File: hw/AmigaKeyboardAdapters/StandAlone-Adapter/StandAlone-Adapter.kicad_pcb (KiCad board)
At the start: 2 copper layers, 78.7 x 58.4 mm, 56 parts, among them J1 RJ10, J2 Conn_02x03_Odd_Even, P1 CONN_01X02, Q1 BSS138, Q2 BSS138, Q3 BSS138, U1 AZ1117-3.3, U3 STM32F401RCTx

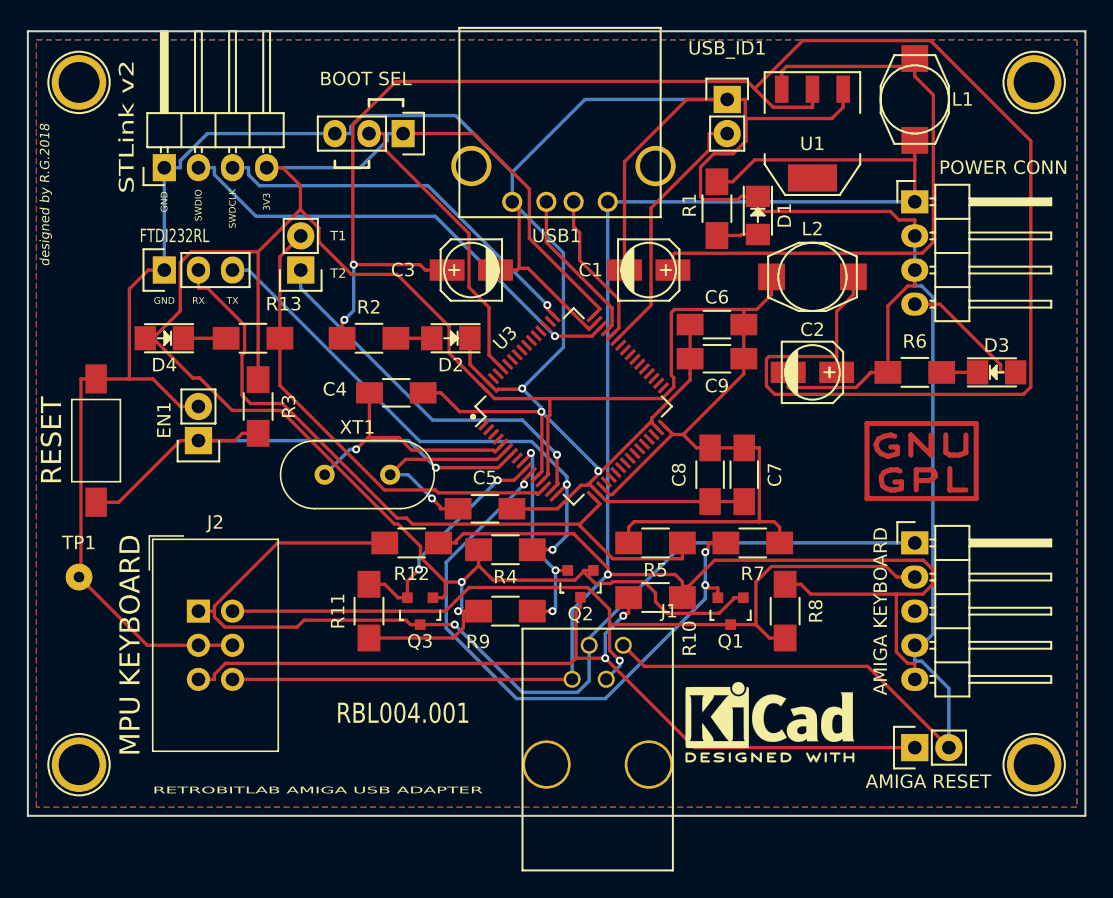
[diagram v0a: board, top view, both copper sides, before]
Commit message: Modified for Capacitors & Added some boot options
Replaced Electrolitic Capacitors with Tantalum ones. Added some
capacitor as in the evaluation board schematics. Added BOOT1 pin. Added
resistors for USB D+ D- lines. Increased the GND trace size to 0.35.
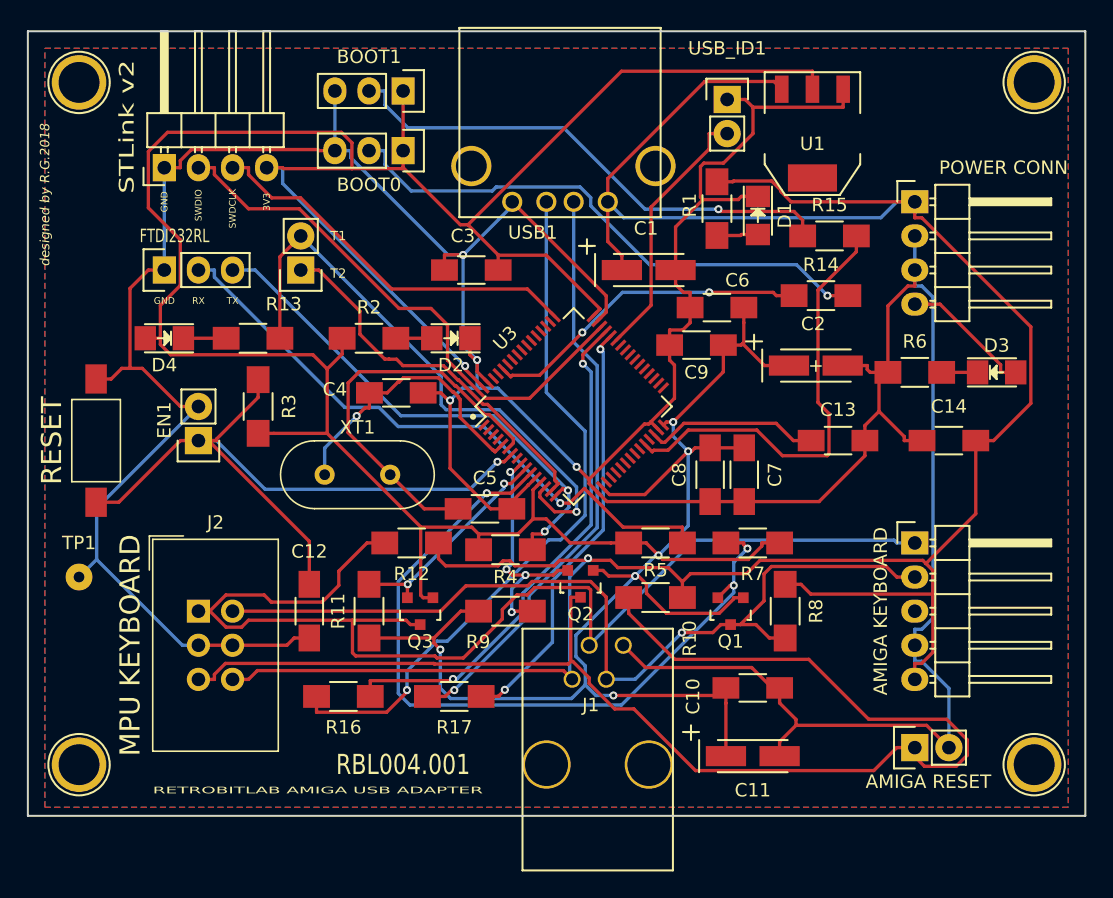
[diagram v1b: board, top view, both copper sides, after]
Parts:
- removed AMIGA: LOGO, RetroBitLab:amigaLogo_BW_31x12mm-SilkScreenBack
- removed GPL: Symbol_GNU-GPL_CopperTop_Small, Symbol:Symbol_GNU-GPL_CopperTop_Small
- removed L1, L2: 10uH, Inductors:SELF-WE-PD3S
- removed WB: LOGO, RetroBitLab:amigaWorkBench1-SIlkScreenBack
- removed kicad: KiCad-Logo2_5mm_SilkScreen, Symbol:KiCad-Logo2_5mm_SilkScreen
- added BOOT0: CONN_01X03, Pin_Headers:Pin_Header_Straight_1x03, F.Cu at (137.2, 74.9)
- added C10: 100n, Capacitors_SMD:C_1206_HandSoldering, F.Cu at (163.2, 114.9)
- added C11: 10u, Capacitors_Tantalum_SMD:TantalC_SizeA_EIA-3216_HandSoldering, F.Cu at (163.2, 120.0)
- added C12: 100n, Capacitors_SMD:C_1206_HandSoldering, F.Cu at (130.2, 109.2)
- added C13: 4.7u, Capacitors_SMD:C_1206_HandSoldering, F.Cu at (169.5, 96.5)
- added C14: 100n, Capacitors_SMD:C_1206_HandSoldering, F.Cu at (177.8, 96.5)
- added G***: LOGO, RetroBitLab:amigaWorkBench1-SIlkScreenBack, B.Cu at (138.4, 110.5)
- added G***: LOGO, RetroBitLab:amigaLogo_BW_31x12mm-SilkScreenBack, B.Cu at (151.1, 87.0)
- added R14: 10K, Resistors_SMD:R_1206_HandSoldering, F.Cu at (168.3, 85.7)
- added R15: 10K, Resistors_SMD:R_1206_HandSoldering, F.Cu at (168.9, 81.3)
- added R16: 12, Resistors_SMD:R_1206_HandSoldering, F.Cu at (132.7, 115.6)
- added R17: 12, Resistors_SMD:R_1206_HandSoldering, F.Cu at (141.0, 115.6)
- C1, C2: footprint Capacitors_SMD:c_elec_4x4.5 -> Capacitors_Tantalum_SMD:TantalC_SizeA_EIA-3216_HandSoldering
- C3: value 47u -> 100n; footprint Capacitors_SMD:c_elec_4x4.5 -> Capacitors_SMD:C_1206_HandSoldering
- R1, R13: value 330 -> 1.5K
- R10, R11, R12, R4, R5, R7, R8, R9: value 10k -> 10K
- R2: value 220 -> 1.5K
- R3: value 10K -> 22K
- R6: value 1K -> 1.5K
- moved BOOT1 3.17 mm to (137.2, 70.5)
- moved C9 1.83 mm to (159.0, 89.4)
- moved C6 1.27 mm to (160.5, 86.6)
- moved C2 0.57 mm to (167.9, 90.9)
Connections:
- AMIGA_KEYBOARD1 pad 5: VCC5V -> +5V
- BOOT1 pad 2: BOOT0 -> BOOT1
- C2 pad 1: Net-(C2-Pad1) -> VCC3V3
- C3 pad 1: Net-(C2-Pad1) -> VCC3V3
- EN1 pad 1: Net-(EN1-Pad1) -> NRST
- J1 pad 1: VCC5V -> +5V
- J2 pad 6: VCC5V -> +5V
- POWER1 pad 1: VCC5V -> +5V
- R1 pad 1: VCC5V -> +5V
- R10 pad 1: VCC5V -> +5V
- R12 pad 1: VCC5V -> +5V
- R2 pad 1: Net-(C2-Pad1) -> VCC3V3
- R3 pad 1: VCC3V3 -> NRST
- R3 pad 2: Net-(EN1-Pad1) -> VCC3V3
- R8 pad 1: VCC5V -> +5V
- RESET1 pad 1: Net-(EN1-Pad1) -> NRST
- U1 pad 2: Net-(C2-Pad1) -> VCC3V3
- U3 pad 28: (no net) -> Net-(R15-Pad2)
- U3 pad 30: (no net) -> Net-(C13-Pad1)
- U3 pad 60: BOOT0 -> Net-(R14-Pad1)
- U3 pad 7: Net-(EN1-Pad1) -> NRST
- USB1 pad 1: VCC5V -> +5V
- USB1 pad 2: USB_N -> Net-(R17-Pad2)
- USB1 pad 3: USB_P -> Net-(R16-Pad2)
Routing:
- net VCC5V: track 165.9 -> 0.00 mm, vias 1 -> 0
- net +5V: track 46.5 -> 195.0 mm, vias 0 -> 1
- net Net-(C2-Pad1): track 139.7 -> 0.00 mm, vias 2 -> 0
- net VCC3V3: track 241.5 -> 309.2 mm, vias 2 -> 7
- net NRST: track 0.00 -> 56.5 mm, vias 0 -> 1
- net Net-(R16-Pad2): track 0.00 -> 52.7 mm, vias 0 -> 1
- net Net-(R17-Pad2): track 0.00 -> 43.7 mm, vias 0 -> 1
- net Net-(EN1-Pad1): track 38.8 -> 0.00 mm, vias 1 -> 0
- net BOOT1: track 0.00 -> 38.1 mm, vias 0 -> 1
- net KBD_RESET: track 67.0 -> 100.9 mm, vias 2 -> 0
- net Net-(R15-Pad2): track 0.00 -> 33.3 mm
- net USB_P: track 11.8 -> 38.7 mm, vias 0 -> 2
- net Net-(R14-Pad1): track 0.00 -> 24.6 mm, vias 0 -> 2
- net USB_N: track 11.6 -> 31.8 mm, vias 0 -> 2
- net BOOT0: track 22.4 -> 41.3 mm, vias 0 -> 1
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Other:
- net class GND: trace_width 0.3 -> 0.35
- board text removed: "BOOT SEL"

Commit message: Modified some logo and silkscreen stuff
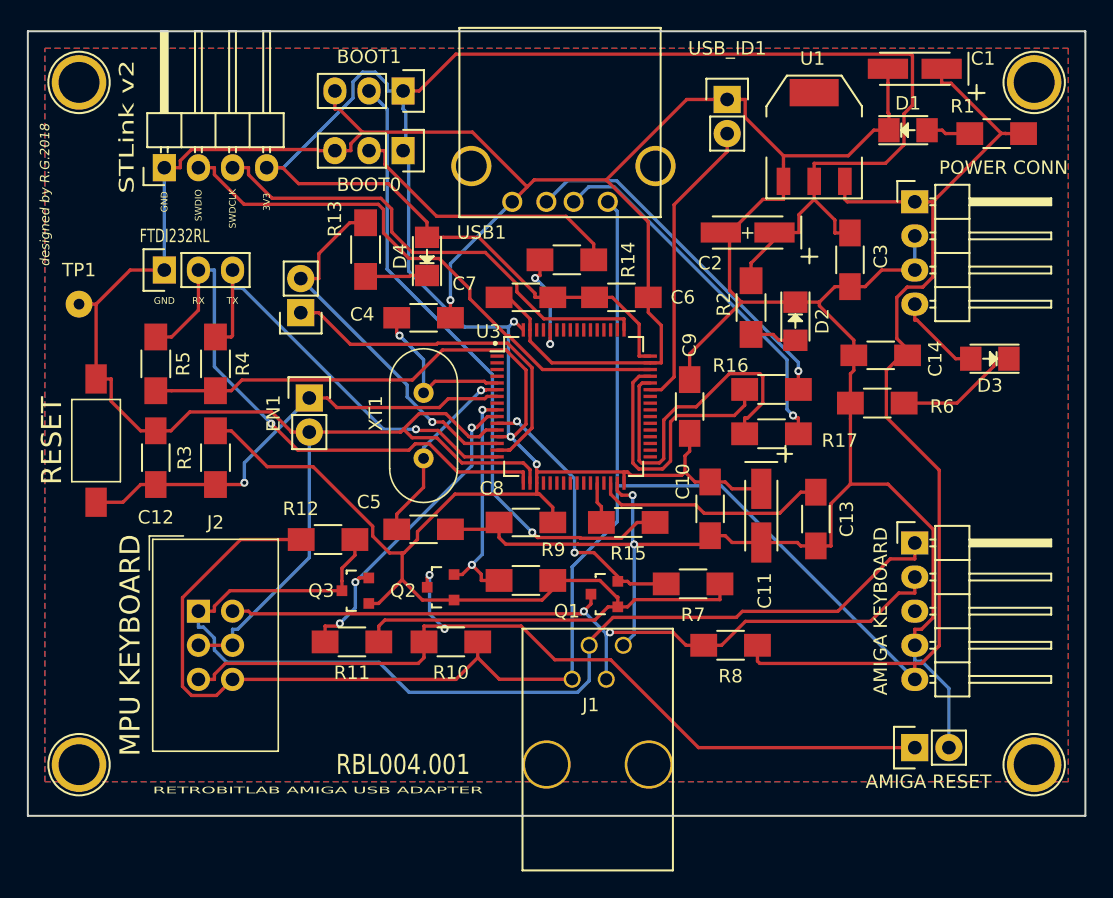
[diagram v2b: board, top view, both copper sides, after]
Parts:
- removed G***: LOGO, RetroBitLab:amigaWorkBench1-SIlkScreenBack
- removed G***: LOGO, RetroBitLab:amigaLogo_BW_31x12mm-SilkScreenBack
- added AMIGALOGO: LOGO, RetroBitLab:amigaLogo_BW_31x12mm, B.Cu at (152.4, 88.9)
- added WBLOGO: LOGO, RetroBitLab:amigaWorkBench1, B.Cu at (154.9, 104.1)
- moved R5 39.5 mm to (118.7, 90.8), turned to 90 degrees
- moved R16 39.2 mm to (164.6, 92.7), turned to 0 degrees
- moved R17 30.7 mm to (164.6, 96.0), turned to 0 degrees
- moved R2 28.5 mm to (163.1, 86.6), turned to 270 degrees
- moved C3 28.2 mm to (170.4, 83.1), turned to 270 degrees
- moved R15 26.1 mm to (153.9, 102.6), turned to 180 degrees
- moved D2 25.7 mm to (166.4, 87.6), turned to 270 degrees
- moved R4 25.6 mm to (123.2, 90.8), turned to 90 degrees
- moved C1 24.8 mm to (175.3, 68.8), turned to 180 degrees
- moved R1 21.6 mm to (181.4, 73.7), turned to 180 degrees
- moved C7 20.9 mm to (146.3, 85.9), turned to 0 degrees
- moved D4 20.5 mm to (138.9, 82.8), turned to 90 degrees
- moved TP1 20.3 mm to (113.0, 86.4)
- moved R14 19.1 mm to (149.4, 83.1)
- moved C11 17.9 mm to (163.8, 102.1), turned to 270 degrees
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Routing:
- net KBD_3v3_DATA: track 57.5 -> 21.2 mm, vias 3 -> 2
- net KBD_RESET: track 100.9 -> 66.0 mm, vias 0 -> 2
- net Net-(R15-Pad2): track 33.3 -> 3.07 mm
- net Net-(R16-Pad2): track 52.7 -> 27.0 mm
- net NRST: track 56.5 -> 34.6 mm
- net BOOT0: track 41.3 -> 21.4 mm, vias 1 -> 0
- net USB_P: track 38.7 -> 20.8 mm, vias 2 -> 0
- net Net-(R14-Pad1): track 24.6 -> 8.04 mm
- net Net-(R17-Pad2): track 43.7 -> 27.7 mm
- net TP1: track 43.8 -> 27.9 mm
- net Net-(C5-Pad1): track 29.9 -> 14.2 mm, vias 0 -> 1
- net BOOT1: track 38.1 -> 47.7 mm
- net Net-(C4-Pad1): track 21.4 -> 12.3 mm
- net KBD_CLOCK: track 88.3 -> 79.8 mm
- net KBD_3v3_CLOCK: track 16.5 -> 24.4 mm, vias 2 -> 3
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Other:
- net class +5V: trace_width 0.3 -> 0.35
- net class Default: trace_width 0.25 -> 0.3
- net class GND: trace_width 0.35 -> 0.4
- net class VCC3V3: trace_width 0.3 -> 0.35
- net class VCC5V: trace_width 0.3 -> 0.35
- board text removed: "T1"
- board text removed: "T2"

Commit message: Added GNU GPL LOGO on silkscreen top
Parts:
- added REF**: Symbol_GNU-GPL_CopperTop_Small, RetroBitLab:Symbol_GNU-GPL_SilkScreen_Small, F.Cu at (177.8, 99.1)
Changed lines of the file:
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@@
     (tracks 646)
     (zones 0)
-    (modules 62)
+    (modules 63)
     (nets 34)
   )
@@
       (xy 1.307739 4.732367)) (layer B.SilkS) (width 0.01))
   )
+  (module RetroBitLab:Symbol_GNU-GPL_SilkScreen_Small (layer F.Cu)
+    (at 177.8 99.06)
+    (descr "Symbol, GNU-GPL, Copper Top, Small,")
+    (tags "Symbol, GNU-GPL, Copper Top, Small,")
+    (fp_text reference REF** (at 0.50038 -6.79958) (layer F.SilkS)
+      (effects (font (size 1 1) (thickness 0.15)))
+    )
+    (fp_text value Symbol_GNU-GPL_CopperTop_Small (at -0.09906 6.10108) (layer F.Fab)
+      (effects (font (size 1 1) (thickness 0.15)))
+    )
+    (fp_line (start 2.10058 0.29972) (end 2.10058 1.89992) (layer F.SilkS) (width 0.381))
+    (fp_line (start 2.10058 1.89992) (end 3.29946 1.89992) (layer F.SilkS) (width 0.381))
+    (fp_line (start -0.39878 1.89992) (end -0.39878 0.39878) (layer F.SilkS) (width 0.381))
+    (fp_line (start -0.39878 0.39878) (end 0.50038 0.39878) (layer F.SilkS) (width 0.381))
+    (fp_line (start 0.50038 0.39878) (end 0.70104 0.39878) (layer F.SilkS) (width 0.381))
+    (fp_line (start 0.70104 0.39878) (end 0.89916 0.50038) (layer F.SilkS) (width 0.381))
+    (fp_line (start 0.89916 0.50038) (end 1.00076 0.70104) (layer F.SilkS) (width 0.381))
+    (fp_line (start 1.00076 0.70104) (end 1.00076 0.89916) (layer F.SilkS) (width 0.381))
+    (fp_line (start 1.00076 0.89916) (end 0.8001 1.09982) (layer F.SilkS) (width 0.381))
+    (fp_line (start 0.8001 1.09982) (end 0.50038 1.19888) (layer F.SilkS) (width 0.381))
+    (fp_line (start 0.50038 1.19888) (end -0.39878 1.19888) (layer F.SilkS) (width 0.381))
+    (fp_line (start -1.6002 0.50038) (end -1.80086 0.39878) (layer F.SilkS) (width 0.381))
+    (fp_line (start -1.80086 0.39878) (end -2.30124 0.39878) (layer F.SilkS) (width 0.381))
+    (fp_line (start -2.30124 0.39878) (end -2.60096 0.50038) (layer F.SilkS) (width 0.381))
+    (fp_line (start -2.60096 0.50038) (end -2.79908 0.59944) (layer F.SilkS) (width 0.381))
+    (fp_line (start -2.79908 0.59944) (end -2.99974 0.89916) (layer F.SilkS) (width 0.381))
+    (fp_line (start -2.99974 0.89916) (end -2.99974 1.19888) (layer F.SilkS) (width 0.381))
+    (fp_line (start -2.99974 1.19888) (end -2.90068 1.6002) (layer F.SilkS) (width 0.381))
+    (fp_line (start -2.90068 1.6002) (end -2.60096 1.80086) (layer F.SilkS) (width 0.381))
+    (fp_line (start -2.60096 1.80086) (end -2.30124 1.89992) (layer F.SilkS) (width 0.381))
+    (fp_line (start -2.30124 1.89992) (end -1.99898 1.89992) (layer F.SilkS) (width 0.381))
+    (fp_line (start -1.99898 1.89992) (end -1.50114 1.80086) (layer F.SilkS) (width 0.381))
+    (fp_line (start -1.50114 1.80086) (end -1.50114 1.30048) (layer F.SilkS) (width 0.381))
+    (fp_line (start -1.50114 1.30048) (end -1.99898 1.30048) (layer F.SilkS) (width 0.381))
+    (fp_line (start 1.80086 -2.19964) (end 1.80086 -0.89916) (layer F.SilkS) (width 0.381))
+    (fp_line (start 1.80086 -0.89916) (end 2.10058 -0.70104) (layer F.SilkS) (width 0.381))
+    (fp_line (start 2.10058 -0.70104) (end 2.4003 -0.70104) (layer F.SilkS) (width 0.381))
+    (fp_line (start 2.4003 -0.70104) (end 2.79908 -0.70104) (layer F.SilkS) (width 0.381))
+    (fp_line (start 2.79908 -0.70104) (end 3.0988 -0.8001) (layer F.SilkS) (width 0.381))
+    (fp_line (start 3.0988 -0.8001) (end 3.29946 -0.89916) (layer F.SilkS) (width 0.381))
+    (fp_line (start 3.29946 -0.89916) (end 3.29946 -2.19964) (layer F.SilkS) (width 0.381))
+    (fp_line (start -0.8001 -0.70104) (end -0.8001 -2.19964) (layer F.SilkS) (width 0.381))
+    (fp_line (start -0.8001 -2.19964) (end 0.70104 -0.70104) (layer F.SilkS) (width 0.381))
+    (fp_line (start 0.70104 -0.70104) (end 0.70104 -2.19964) (layer F.SilkS) (width 0.381))
+    (fp_line (start -1.99898 -2.10058) (end -2.30124 -2.19964) (layer F.SilkS) (width 0.381))
+    (fp_line (start -2.30124 -2.19964) (end -2.79908 -2.10058) (layer F.SilkS) (width 0.381))
+    (fp_line (start -2.79908 -2.10058) (end -3.2004 -1.89992) (layer F.SilkS) (width 0.381))
+    (fp_line (start -3.2004 -1.89992) (end -3.40106 -1.50114) (layer F.SilkS) (width 0.381))
+    (fp_line (start -3.40106 -1.50114) (end -3.29946 -1.09982) (layer F.SilkS) (width 0.381))
+    (fp_line (start -3.29946 -1.09982) (end -2.99974 -0.8001) (layer F.SilkS) (width 0.381))
+    (fp_line (start -2.99974 -0.8001) (end -2.49936 -0.59944) (layer F.SilkS) (width 0.381))
+    (fp_line (start -2.49936 -0.59944) (end -1.80086 -0.8001) (layer F.SilkS) (width 0.381))
+    (fp_line (start -1.80086 -0.8001) (end -1.80086 -1.30048) (layer F.SilkS) (width 0.381))
+    (fp_line (start -1.80086 -1.30048) (end -2.30124 -1.30048) (layer F.SilkS) (width 0.381))
+    (fp_line (start -4.064 -3.048) (end 4.064 -3.048) (layer F.SilkS) (width 0.381))
+    (fp_line (start 4.064 -3.048) (end 4.064 2.54) (layer F.SilkS) (width 0.381))
+    (fp_line (start 4.064 2.54) (end -4.064 2.54) (layer F.SilkS) (width 0.381))
+    (fp_line (start -4.064 2.54) (end -4.064 -3.048) (layer F.SilkS) (width 0.381))
+  )
   (gr_circle (center 144.018 89.281) (end 143.9545 89.2175) (layer F.SilkS) (width 0.2))

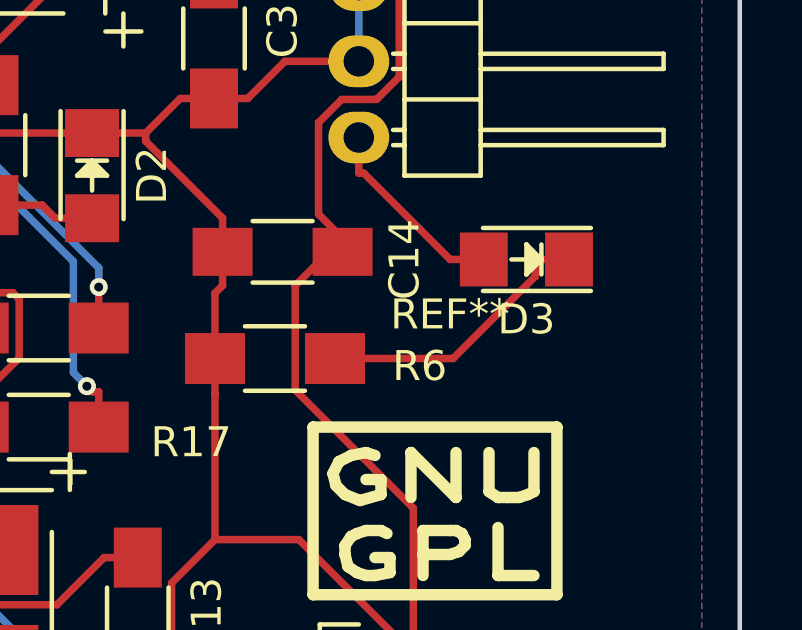
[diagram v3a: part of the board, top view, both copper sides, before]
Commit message: Changed the capacitors for Crystal Oscillator. From 22pf to 20pf for 8Mhz
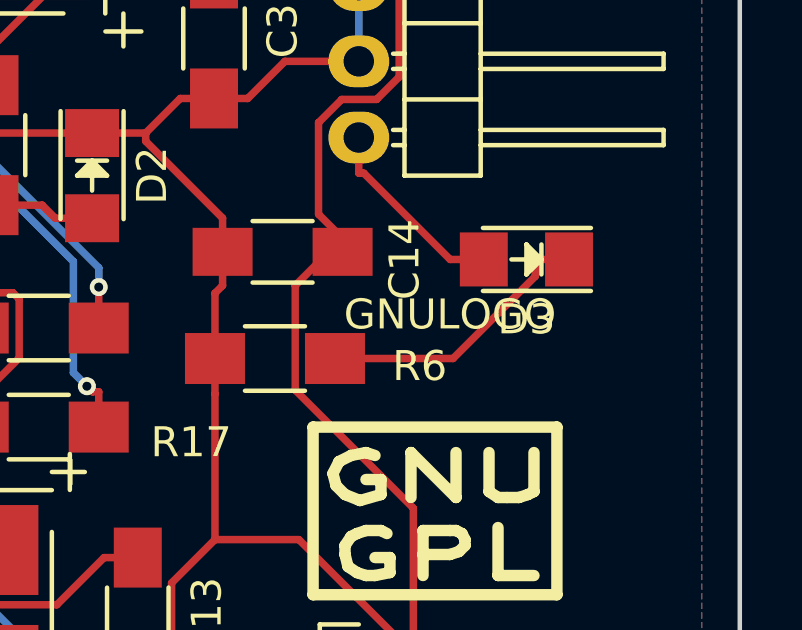
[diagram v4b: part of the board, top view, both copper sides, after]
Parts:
- C4, C5: value 22p -> 20p
- R16, R17: value 12 -> 12ohm
- renumbered REF** to GNULOGO
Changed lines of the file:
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@@
       (effects (font (size 1 1) (thickness 0.15)))
     )
-    (fp_text value 22p (at 0 2.3) (layer F.Fab)
+    (fp_text value 20p (at 0 2.3) (layer F.Fab)
       (effects (font (size 1 1) (thickness 0.15)))
     )
@@
       (effects (font (size 1 1) (thickness 0.15)))
     )
-    (fp_text value 22p (at 0 2.3) (layer F.Fab)
+    (fp_text value 20p (at 0 2.3) (layer F.Fab)
       (effects (font (size 1 1) (thickness 0.15)))
     )
@@
       (effects (font (size 1 1) (thickness 0.15)))
     )
-    (fp_text value 12 (at 0 2.3) (layer F.Fab)
+    (fp_text value 12ohm (at 0 2.3) (layer F.Fab)
       (effects (font (size 1 1) (thickness 0.15)))
     )
@@
       (effects (font (size 1 1) (thickness 0.15)))
     )
-    (fp_text value 12 (at 0 2.3) (layer F.Fab)
+    (fp_text value 12ohm (at 0 2.3) (layer F.Fab)
       (effects (font (size 1 1) (thickness 0.15)))
     )
@@
     (descr "Symbol, GNU-GPL, Copper Top, Small,")
     (tags "Symbol, GNU-GPL, Copper Top, Small,")
-    (fp_text reference REF** (at 0.50038 -6.79958) (layer F.SilkS)
-      (effects (font (size 1 1) (thickness 0.15)))
-    )
+    (fp_text reference GNULOGO (at 0.50038 -6.79958) (layer F.SilkS)
+      (effects (font (size 1 1) (thickness 0.15)))
+    )
